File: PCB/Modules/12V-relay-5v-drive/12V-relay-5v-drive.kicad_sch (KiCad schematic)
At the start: 4 parts, among them J1 Screw_Terminal_01x02, K1 AWHSH112DM00G, U1 ULN2003A

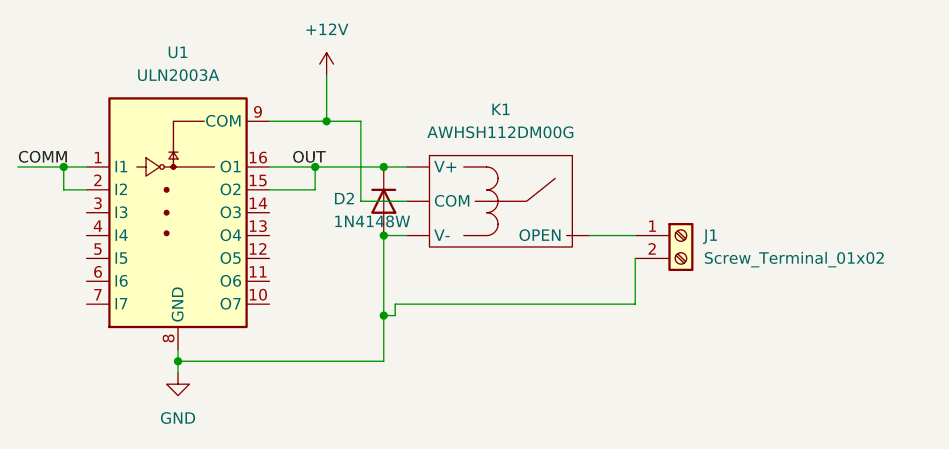
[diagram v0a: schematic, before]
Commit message: Added switch modules and RS485 module
Signed-off-by: Simonca Raul <simonca.raul@gmail.com>
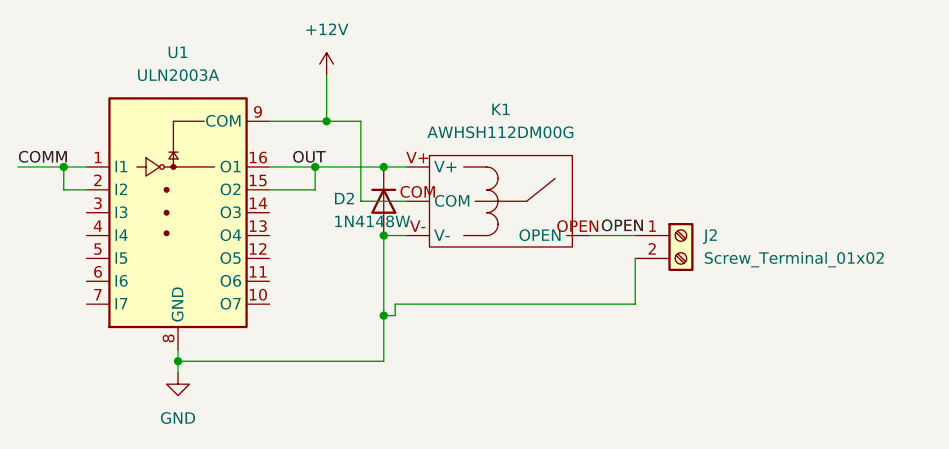
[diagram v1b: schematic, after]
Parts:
- removed J1: Screw_Terminal_01x02, TerminalBlock:TerminalBlock_Xinya_XY308-2.54-2P_1x02_P2.54mm_Horizontal, symbol Connector:Screw_Terminal_01x02
- added J2: Screw_Terminal_01x02, TerminalBlock:TerminalBlock_bornier-2_P5.08mm, symbol Connector:Screw_Terminal_01x02
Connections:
- net +12V: now also K1.COM; no longer K1. (V-)
- net GND: now also K1.V-, J2.2 (Pin_2); no longer K1. (V-)
- net OUT: now also K1.V+; no longer K1. (V-)
- new net OPEN: J2.1 (Pin_1), K1.OPEN
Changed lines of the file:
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@@
+	(wire
+		(pts
+			(xy 160.02 92.71) (xy 165.1 92.71)
+		)
+		(stroke
+			(width 0)
+			(type default)
+		)
+	)
 	(wire
 		(pts
@@
 		(pts
 			(xy 137.16 106.68) (xy 114.3 106.68)
-		)
-		(stroke
-			(width 0)
-			(type default)
-		)
-	)
-	(wire
-		(pts
-			(xy 160.02 92.71) (xy 165.1 92.71)
 		)
 		(stroke
@@
 		)
 	)
-	(symbol
-		(lib_id "Connector:Screw_Terminal_01x02")
-		(at 170.18 92.71 0)
-		(unit 1)
-		(exclude_from_sim no)
-		(in_bom yes)
-		(on_board yes)
-		(dnp no)
-		(fields_autoplaced yes)
-		(property "Reference" "J1"
-			(at 172.72 92.7099 0)
-			(effects
-				(font
-					(size 1.27 1.27)
-				)
-				(justify left)
-			)
-		)
-		(property "Value" "Screw_Terminal_01x02"
-			(at 172.72 95.2499 0)
-			(effects
-				(font
-					(size 1.27 1.27)
-				)
-				(justify left)
-			)
-		)
-		(property "Footprint" "TerminalBlock:TerminalBlock_Xinya_XY308-2.54-2P_1x02_P2.54mm_Horizontal"
-			(at 170.18 92.71 0)
-			(effects
-				(font
-					(size 1.27 1.27)
-				)
-				(hide yes)
-			)
-		)
-		(property "Datasheet" "~"
-			(at 170.18 92.71 0)
-			(effects
-				(font
-					(size 1.27 1.27)
-				)
-				(hide yes)
-			)
-		)
-		(property "Description" "Generic screw terminal, single row, 01x02, script generated (kicad-library-utils/schlib/autogen/connector/)"
-			(at 170.18 92.71 0)
-			(effects
-				(font
-					(size 1.27 1.27)
-				)
-				(hide yes)
-			)
-		)
-		(pin "1"
-		)
-		(pin "2"
-		)
-		(instances
-			(project ""
-				(path "/d710513c-5f39-4905-b96f-4745a603cd73"
-					(reference "J1")
-					(unit 1)
-				)
-			)
+	(label "OPEN"
+		(at 161.29 92.71 0)
+		(fields_autoplaced yes)
+		(effects
+			(font
+				(size 1.27 1.27)
+			)
+			(justify left bottom)
 		)
 	)
@@
 	)
 	(symbol
+		(lib_id "power:+12V")
+		(at 130.81 74.93 0)
+		(unit 1)
+		(exclude_from_sim no)
+		(in_bom yes)
+		(on_board yes)
+		(dnp no)
+		(fields_autoplaced yes)
+		(property "Reference" "#PWR01"
+			(at 130.81 78.74 0)
+			(effects
+				(font
+					(size 1.27 1.27)
+				)
+				(hide yes)
+			)
+		)
+		(property "Value" "+12V"
+			(at 130.81 69.85 0)
+			(effects
+				(font
+					(size 1.27 1.27)
+				)
+			)
+		)
+		(property "Footprint" ""
+			(at 130.81 74.93 0)
+			(effects
+				(font
+					(size 1.27 1.27)
+				)
+				(hide yes)
+			)
+		)
+		(property "Datasheet" ""
+			(at 130.81 74.93 0)
+			(effects
+				(font
+					(size 1.27 1.27)
+				)
+				(hide yes)
+			)
+		)
+		(property "Description" "Power symbol creates a global label with name \"+12V\""
+			(at 130.81 74.93 0)
+			(effects
+				(font
+					(size 1.27 1.27)
+				)
+				(hide yes)
+			)
+		)
+		(pin "1"
+		)
+		(instances
+			(project ""
+				(path "/d710513c-5f39-4905-b96f-4745a603cd73"
+					(reference "#PWR01")
+					(unit 1)
+				)
+			)
+		)
+	)
+	(symbol
 		(lib_id "Relay:AWHSH112DM00G")
 		(at 149.86 88.9 0)
@@
 			)
 		)
-		(pin ""
-		)
-		(pin ""
-		)
-		(pin ""
-		)
-		(pin ""
+		(pin "V+"
+		)
+		(pin "V-"
+		)
+		(pin "OPEN"
+		)
+		(pin "COM"
 		)
 		(instances
@@
 				(path "/d710513c-5f39-4905-b96f-4745a603cd73"
 					(reference "K1")
-					(unit 1)
-				)
-			)
-		)
-	)
-	(symbol
-		(lib_id "power:+12V")
-		(at 130.81 74.93 0)
-		(unit 1)
-		(exclude_from_sim no)
-		(in_bom yes)
-		(on_board yes)
-		(dnp no)
-		(fields_autoplaced yes)
-		(property "Reference" "#PWR01"
-			(at 130.81 78.74 0)
-			(effects
-				(font
-					(size 1.27 1.27)
-				)
-				(hide yes)
-			)
-		)
-		(property "Value" "+12V"
-			(at 130.81 69.85 0)
-			(effects
-				(font
-					(size 1.27 1.27)
-				)
-			)
-		)
-		(property "Footprint" ""
-			(at 130.81 74.93 0)
-			(effects
-				(font
-					(size 1.27 1.27)
-				)
-				(hide yes)
-			)
-		)
-		(property "Datasheet" ""
-			(at 130.81 74.93 0)
-			(effects
-				(font
-					(size 1.27 1.27)
-				)
-				(hide yes)
-			)
-		)
-		(property "Description" "Power symbol creates a global label with name \"+12V\""
-			(at 130.81 74.93 0)
-			(effects
-				(font
-					(size 1.27 1.27)
-				)
-				(hide yes)
-			)
-		)
-		(pin "1"
-		)
-		(instances
-			(project ""
-				(path "/d710513c-5f39-4905-b96f-4745a603cd73"
-					(reference "#PWR01")
 					(unit 1)
 				)
@@
 					(unit 1)
 				)
+			)
+		)
+	)
+	(symbol
+		(lib_id "Connector:Screw_Terminal_01x02")
+		(at 170.18 92.71 0)
+		(unit 1)
+		(exclude_from_sim no)
+		(in_bom yes)
+		(on_board yes)
+		(dnp no)
+		(fields_autoplaced yes)
+		(property "Reference" "J2"
+			(at 172.72 92.7099 0)
+			(effects
+				(font
+					(size 1.27 1.27)
+				)
+				(justify left)
+			)
+		)
+		(property "Value" "Screw_Terminal_01x02"
+			(at 172.72 95.2499 0)
+			(effects
+				(font
+					(size 1.27 1.27)
+				)
+				(justify left)
+			)
+		)
+		(property "Footprint" "TerminalBlock:TerminalBlock_bornier-2_P5.08mm"
+			(at 170.18 92.71 0)
+			(effects
+				(font
+					(size 1.27 1.27)
+				)
+				(hide yes)
+			)
+		)
+		(property "Datasheet" "~"
+			(at 170.18 92.71 0)
+			(effects
+				(font
+					(size 1.27 1.27)
+				)
+				(hide yes)
+			)
+		)
+		(property "Description" "Generic screw terminal, single row, 01x02, script generated (kicad-library-utils/schlib/autogen/connector/)"
+			(at 170.18 92.71 0)
+			(effects
+				(font
+					(size 1.27 1.27)
+				)
+				(hide yes)
+			)
+		)
+		(pin "1"
+		)
+		(pin "2"
+		)
+		(instances
+			(project ""
+				(path "/d710513c-5f39-4905-b96f-4745a603cd73"
+					(reference "J2")
+					(unit 1)
+				)
